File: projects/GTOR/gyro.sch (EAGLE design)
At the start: 6 parts, among them IC1 ISM330DHCXTR

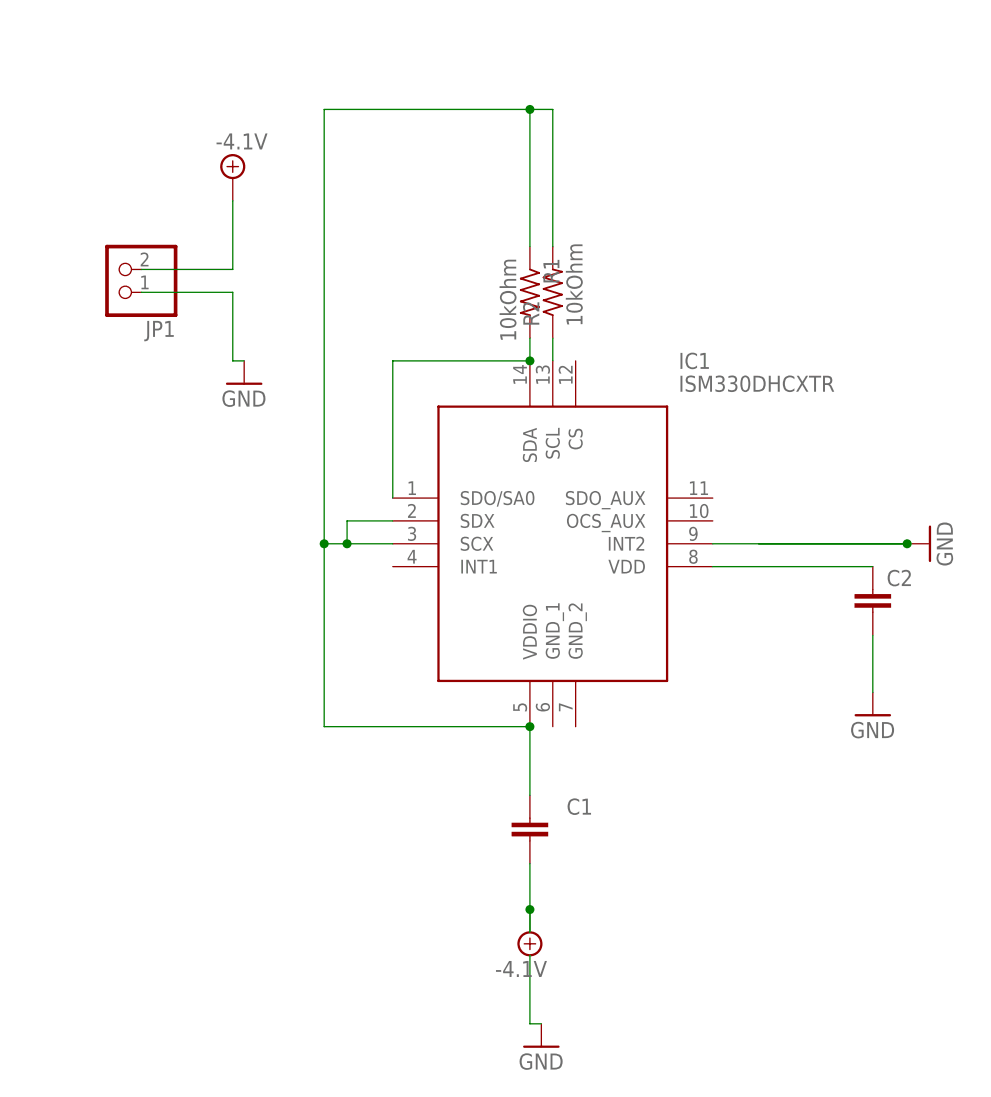
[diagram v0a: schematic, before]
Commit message: Added chip select pin
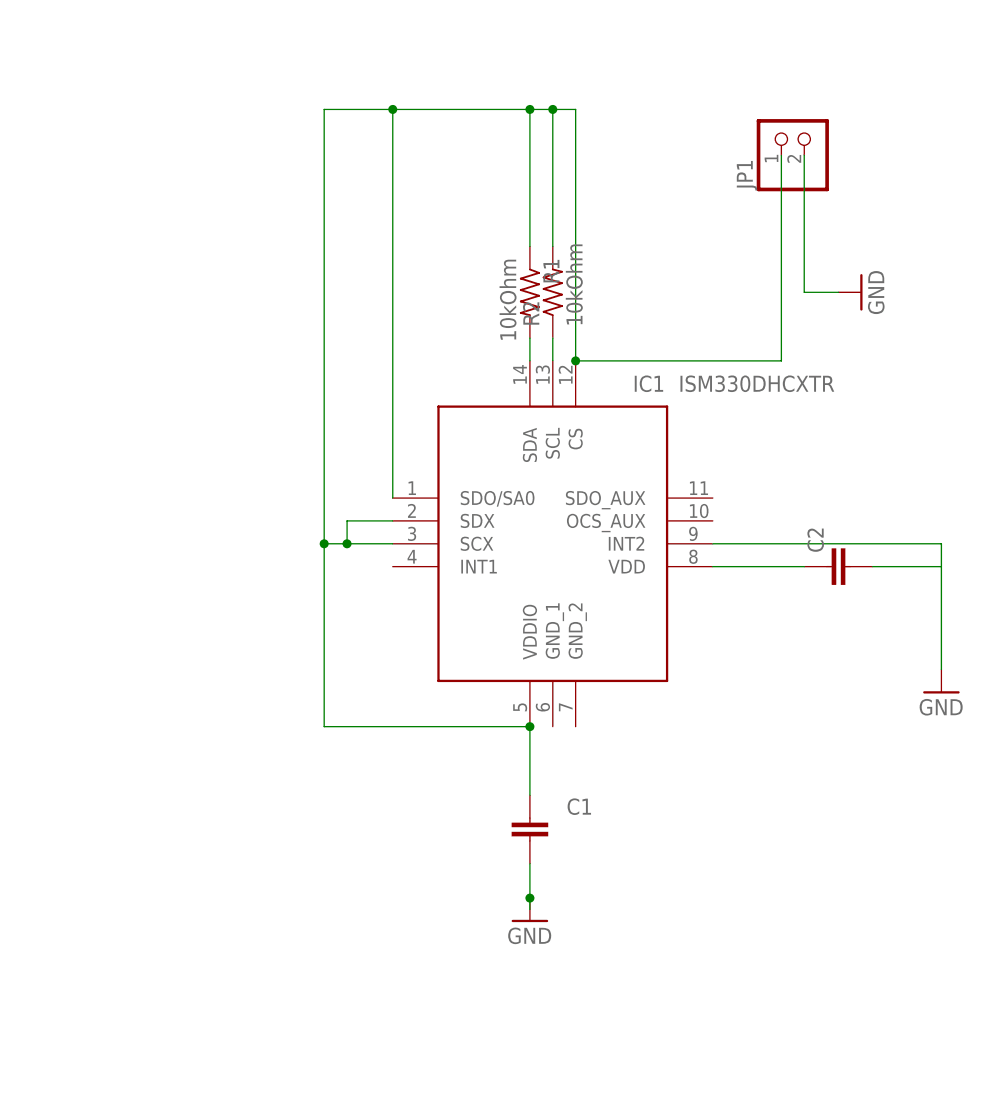
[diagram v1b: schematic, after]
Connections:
- removed net -4.1V: C1.2, JP1.2
- removed net N$1: C1.1, IC1.SCX, IC1.SDX, IC1.VDDIO, R1.1, R2.2
- removed net N$6: JP1.1
- new net N$5: IC1.SDA, R1.2
- net GND: now also C1.2, JP1.2
- net N$2: now also C1.1, IC1.CS, IC1.SCX, IC1.SDX, IC1.VDDIO, JP1.1, R1.1, R2.2; no longer IC1.SDA, R1.2
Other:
- moved on the sheet: C2, JP1

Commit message: added pin header
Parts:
- removed JP1: (no value), pinhead:PINHD-1X2
- added J1: 19428-0004, SamacSys_Parts:19428-0004
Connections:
- new net N$1: IC1.CS, IC1.SCX, IC1.SDO/SA0, IC1.SDX, J1.4, J1.5, R1.1, R2.2
- new net N$6: C1.1, IC1.VDDIO, J1.3
- net GND: now also J1.6; no longer C2.2, JP1.2
- net N$2: now also C2.2, IC1.GND_2; no longer C1.1, IC1.CS, IC1.SCX, IC1.SDO/SA0, IC1.SDX, IC1.VDDIO, JP1.1, R1.1, R2.2
